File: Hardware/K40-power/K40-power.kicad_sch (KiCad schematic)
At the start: 15 parts, among them P1 TCB_4, P2 TCB_6, P3 TCB_4

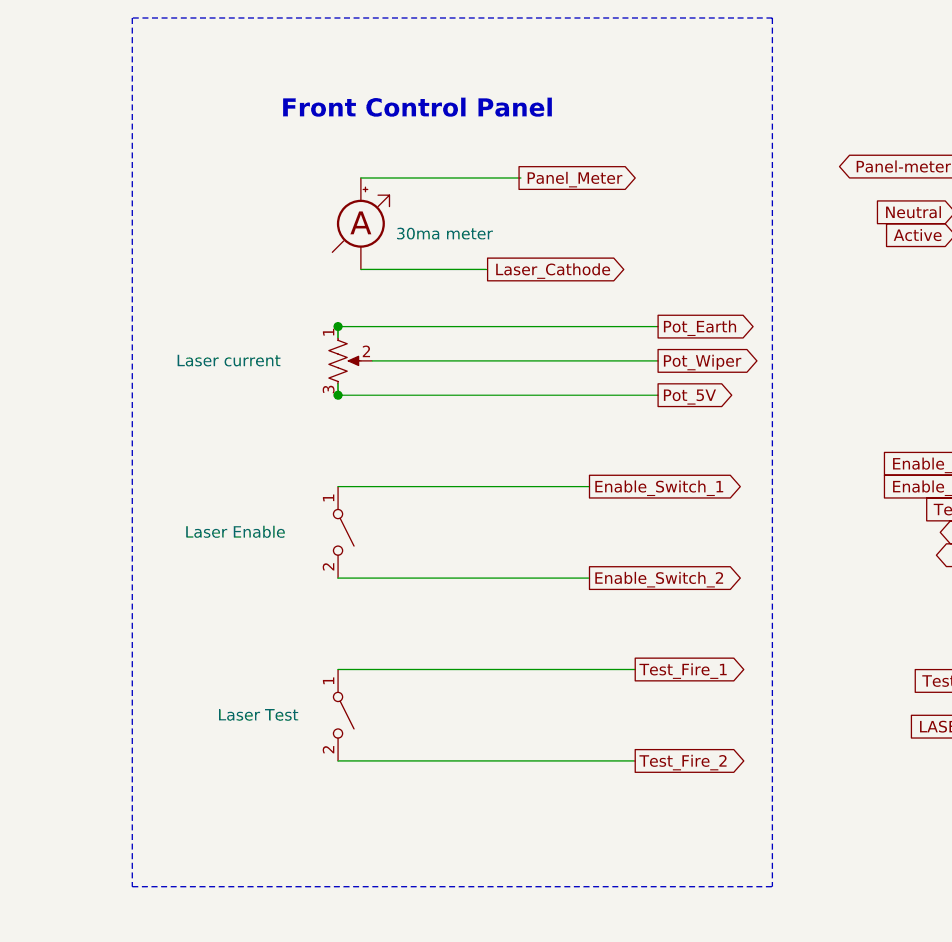
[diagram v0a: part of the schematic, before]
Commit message: Added PDF of schematic
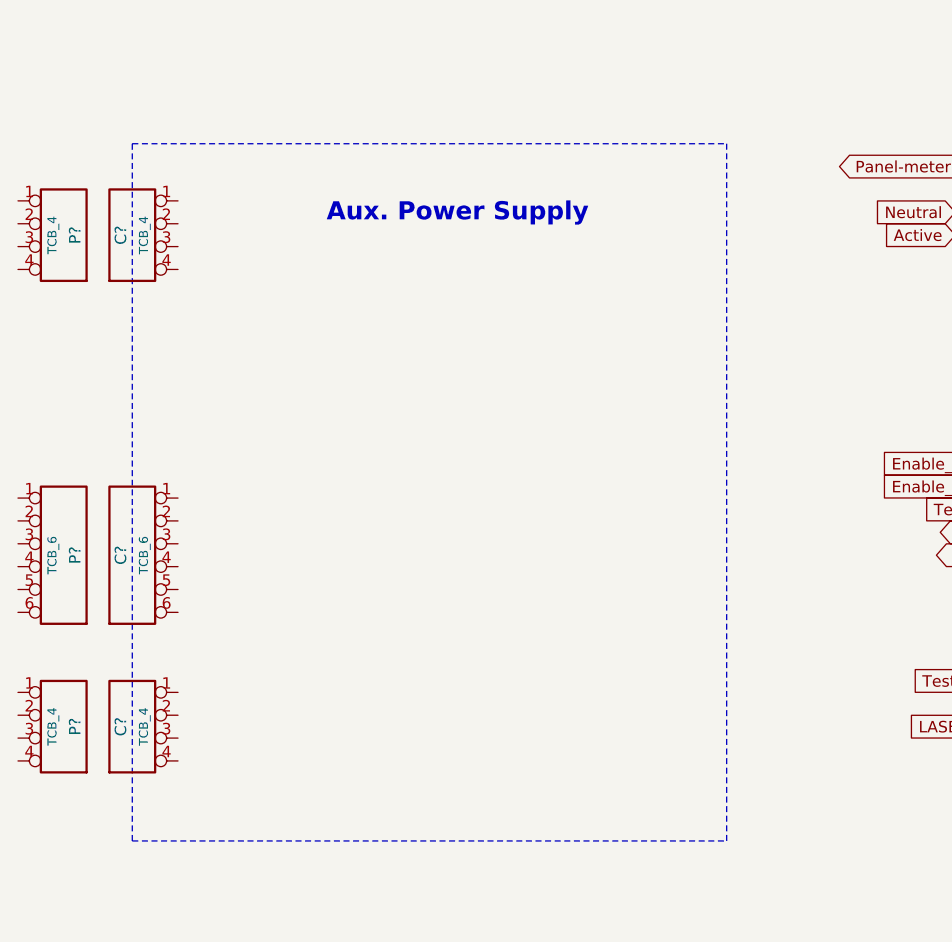
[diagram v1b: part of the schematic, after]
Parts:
- removed MES?: 30ma meter, symbol Device:Amperemeter_DC
- removed RV1: Laser current, symbol Device:R_POT_US
- removed SW?: Laser Enable, symbol Switch:SW_DPST_x2
- removed SW?: Laser Test, symbol Switch:SW_DPST_x2
- added C? (x2), P? (x2): TCB_4, symbol K40-power-rescue:TCB_4-k40-laser
- added C?, P?: TCB_6, symbol K40-power-rescue:TCB_6-k40-laser
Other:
- note added: "Aux. Power Supply"
- note removed: "Front Control Panel"
- company: Geoff Steer -> Hobart Makers

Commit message: Changes to interface PCB layout - test
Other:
- note added: "24V 12V 5V"
- note added: "Connections on front panel"
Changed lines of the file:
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@@
   (junction (at 219.71 115.57) (diameter 1.016) (color 0 0 0 0))
   (junction (at 231.14 104.14) (diameter 1.016) (color 0 0 0 0))
+  (wire (pts (xy 129.54 66.04) (xy 129.54 68.58))
+    (stroke (width 0) (type solid) (color 0 0 0 0))
+  )
   (wire (pts (xy 143.51 58.42) (xy 184.15 58.42))
     (stroke (width 0) (type solid) (color 0 0 0 0))
@@
     (stroke (width 0) (type dash) (color 0 0 0 0))
   )
+  (polyline (pts (xy 128.27 85.09) (xy 128.27 118.11))
+    (stroke (width 0) (type dash) (color 0 0 0 0))
+  )
+  (polyline (pts (xy 128.27 85.09) (xy 163.83 85.09))
+    (stroke (width 0) (type dash) (color 0 0 0 0))
+  )
+  (polyline (pts (xy 163.83 85.09) (xy 163.83 118.11))
+    (stroke (width 0) (type dash) (color 0 0 0 0))
+  )
+  (polyline (pts (xy 163.83 118.11) (xy 128.27 118.11))
+    (stroke (width 0) (type dash) (color 0 0 0 0))
+  )
   (polyline (pts (xy 196.85 52.07) (xy 262.89 52.07))
     (stroke (width 0) (type dash) (color 0 0 0 0))
@@
     (stroke (width 0) (type dash) (color 0 0 0 0))
   )
-  (text "Aux. Power Supply" (at 73.66 64.77 0)
+  (text "Aux. Power Supply\n\n" (at 71.12 72.39 0)
     (effects (font (size 2.0066 2.0066) (thickness 0.4013) bold) (justify left bottom))
+  )
+  (text "24V\n12V\n5V" (at 80.01 80.01 0)
+    (effects (font (size 1.27 1.27)) (justify left bottom))
+  )
+  (text "Connections on front panel" (at 133.35 87.63 0)
+    (effects (font (size 1.27 1.27)) (justify left bottom))
   )
   (text "Laser Power Supply" (at 218.44 60.96 0)
@@
     (pin "2")
   )
+  (symbol (lib_id "power:AC") (at 129.54 68.58 0) (unit 1)
+    (in_bom yes) (on_board yes) (fields_autoplaced)
+    (property "Reference" "#PWR?" (id 0) (at 129.54 71.12 0)
+      (effects (font (size 1.27 1.27)) hide)
+    )
+    (property "Value" "AC" (id 1) (at 129.54 62.3084 0))
+    (property "Footprint" "" (id 2) (at 129.54 68.58 0)
+      (effects (font (size 1.27 1.27)) hide)
+    )
+    (property "Datasheet" "" (id 3) (at 129.54 68.58 0)
+      (effects (font (size 1.27 1.27)) hide)
+    )
+    (pin "1")
+  )
   (symbol (lib_id "power:Earth_Protective") (at 163.83 67.31 0) (unit 1)
     (in_bom yes) (on_board yes)
@@
       (reference "#PWR?") (unit 1) (value "+5V") (footprint "")
     )
+    (path "/9d35feb6-5829-472d-a9b9-406973315324"
+      (reference "#PWR?") (unit 1) (value "AC") (footprint "")
+    )
     (path "/00000000-0000-0000-0000-000060542e9d"

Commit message: Changes to be committed: 	new file:   K40-panel/K40-panel-switch.kicad_sch 	modified:   K40-panel/K40-panel.kicad_sch 	modified:   K40-panel/switch.kicad_sch Renamed to K40-panel-switch.kicad_sch 	modified:   K40-power/K40-power.kicad_prl 	modified:   K40-power/K40-power.kicad_sch Updated symbols, added notes about auxillary power supply
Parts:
- removed C? (x2), P? (x2): TCB_4, symbol K40-power-rescue:TCB_4-k40-laser
- removed P?: TCB_6, symbol K40-power-rescue:TCB_6-k40-laser
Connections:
- net Active: now also C?.2 (P)
- net Earth_Protective: now also C?.3 (P)
- net Neutral: now also C?.1 (P)
- net 24V: now reaches C?.5 (P)
- net 12V: now reaches C?.6 (P)
- new net 5V: C?.8 (P)
- new net COM: C?.7 (P)
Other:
- note added: "NOTE: COMMON is not connected to frame ground."
- moved on the sheet: C1, C2, C3, P1, P2, P3

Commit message: modified:   Hardware/K40-panel/K40-panel.kicad_sch 	modified:   Hardware/K40-panel/switch.kicad_sch Updated labels 	modified:   Hardware/K40-power/K40-power.kicad_sch CLeaned up auxillary power diagram
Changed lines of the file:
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@@
     )
   )
-  (global_label "Pot_Wiper" (shape output) (at 118.11 76.2 180) (fields_autoplaced)
+  (global_label "Pot_Wiper" (shape input) (at 118.11 76.2 180) (fields_autoplaced)
     (effects (font (size 1.27 1.27)) (justify right))
-    (property "Intersheet References" "${INTERSHEET_REFS}" (id 0) (at -34.29 -25.4 0)
-      (effects (font (size 1.27 1.27)) hide)
+    (property "Intersheet References" "${INTERSHEET_REFS}" (id 0) (at 106.5045 76.1206 0)
+      (effects (font (size 1.27 1.27)) (justify right) hide)
     )
   )
@@
     (pin "1")
   )
-  (symbol (lib_id "power:+5V") (at 187.96 53.34 0) (unit 1)
+  (symbol (lib_name "+5V_1") (lib_id "power:+5V") (at 187.96 53.34 0) (unit 1)
     (in_bom yes) (on_board yes)
     (property "Reference" "#PWR?" (id 0) (at 187.96 57.15 0)
